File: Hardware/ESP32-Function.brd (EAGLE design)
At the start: 65 x 38.1 mm, 42 parts, among them J1 MICROMOD_STANDARD, Q2 MBT3904DW1T1, U1 EEPROM, U2 ESP-WROOM-3232D-NARROW, U3 3.3V, U4 CP210X

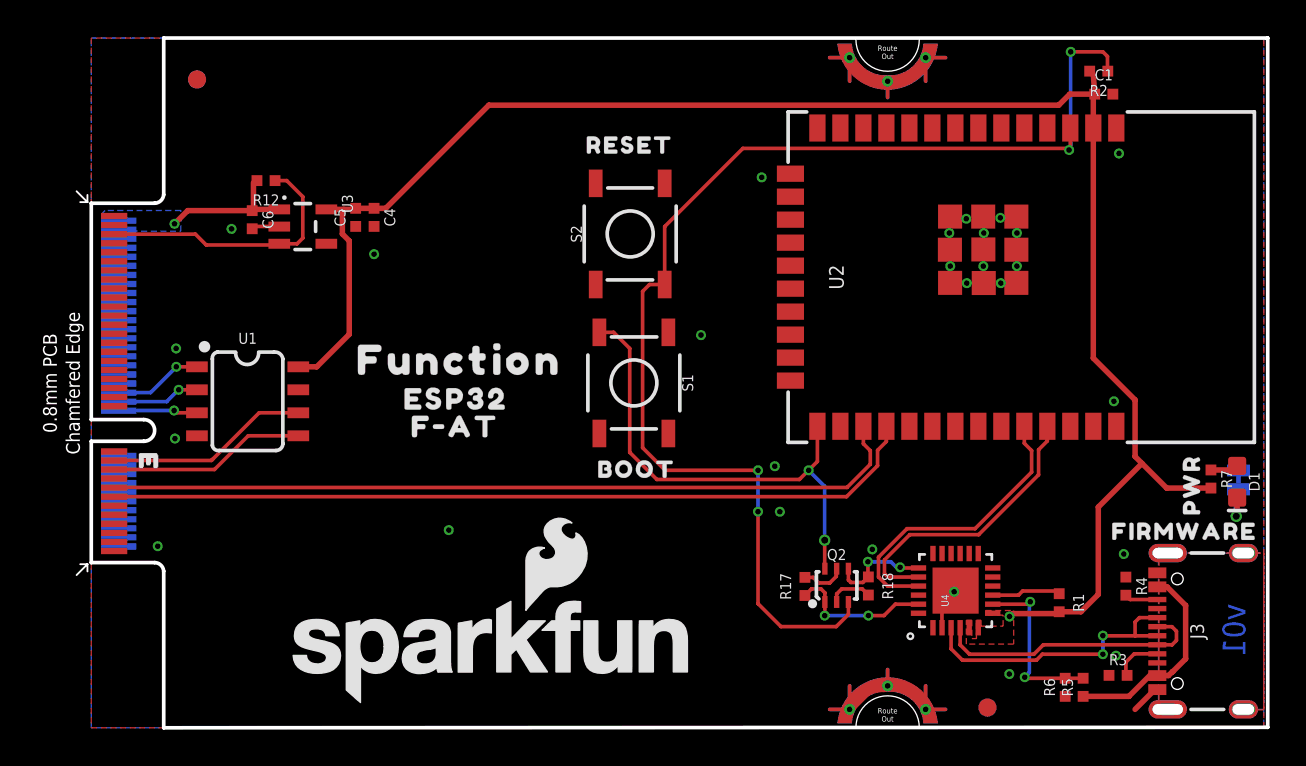
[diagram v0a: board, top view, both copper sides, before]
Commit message: Moves to 0603 components where able, adds silk, fixes traces affected by move to 0603
* removes wire stubs
* Fixes random air wires
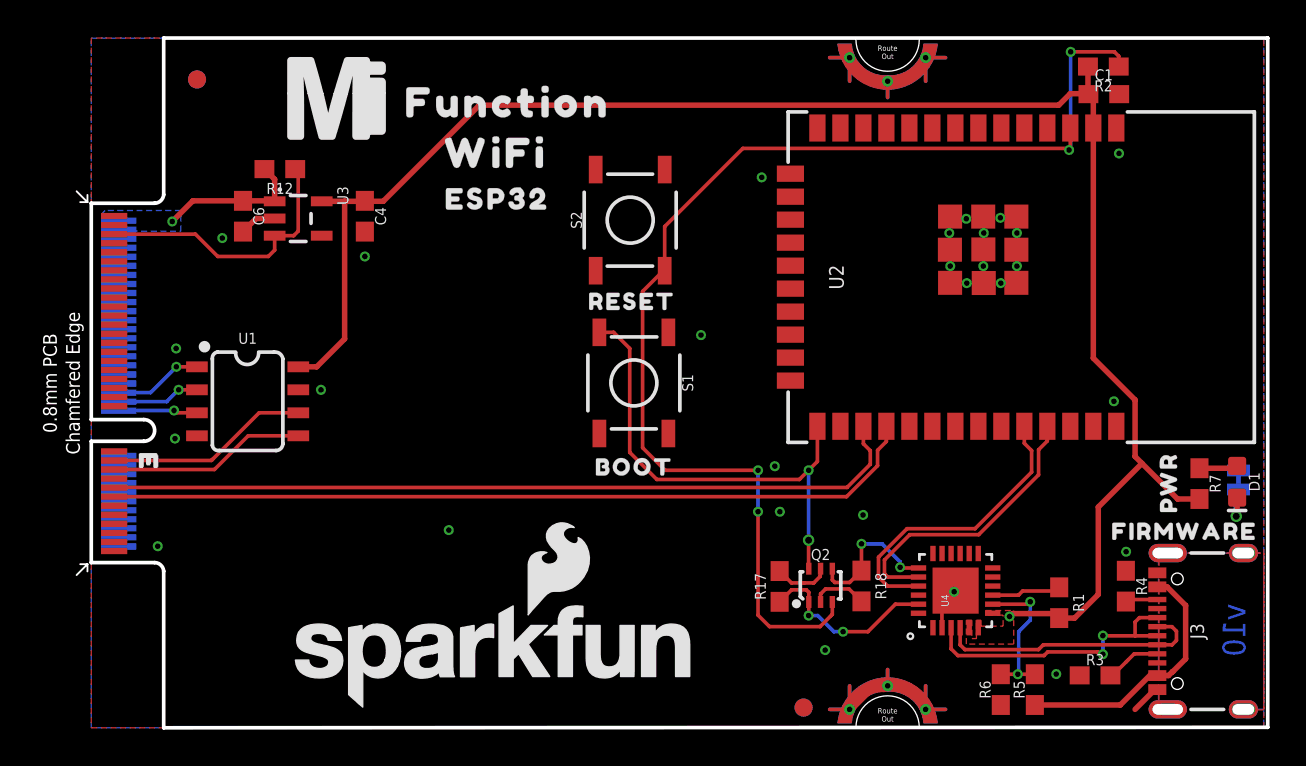
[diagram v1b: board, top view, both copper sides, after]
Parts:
- removed C5: 0.1uF, SparkFun-Capacitors:0402-TIGHT
- removed U$3: (no value), top:F#AT3213
- added U$10: (no value), top:WIFI525
- added U$6: (no value), SparkFun-MicroMod:MICROMOD_MI_LOGO_1
- C1, C6: device SparkFun-Capacitors:0402-TIGHT -> SparkFun-Capacitors:0603
- C4: value 0.1uF -> 1.0uF; device SparkFun-Capacitors:0402-TIGHT -> SparkFun-Capacitors:0603
- D1: device SparkFun-MicroMod-Function:LED-0603 -> SparkFun-LED:LED-0603
- R1, R12, R17, R18, R2, R3, R4, R5, R6, R7: device SparkFun-Resistors:0402-TIGHT -> SparkFun-Resistors:0603
- moved U$2 14.5 mm to (23.0, 34.5)
- moved U$4 11.3 mm to (22.4, 29.2)
- moved FD2 10.2 mm to (39.3, 1.12)
- moved FD4 10.2 mm to (39.3, 1.12)
- moved U$5 8.64 mm to (29.9, 23.5)
- moved R6 3.56 mm to (50.2, 2.11)
- moved R5 2.67 mm to (52.1, 2.11)
- moved R17 1.40 mm to (38.0, 7.81)
- moved U$9 1.28 mm to (59.5, 13.5)
- moved R3 1.27 mm to (55.4, 2.90)
- moved R12 0.99 mm to (10.4, 30.9)
- moved Q2 0.89 mm to (40.3, 7.87)
- moved TP2 0.89 mm to (39.6, 10.4)
- moved S2 0.76 mm to (29.8, 28.0)
- moved R7 0.68 mm to (61.2, 13.5)
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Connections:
- net 3.3V: no longer C5.2
- net GND: no longer C5.1
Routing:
- net N$3: track 11.5 -> 14.4 mm
- net DTR: track 8.05 -> 10.3 mm
- net RTS: track 5.69 -> 7.92 mm
- net N$4: track 9.67 -> 8.29 mm
- net N$12: track 2.45 -> 3.10 mm
- net N$10: track 2.44 -> 3.10 mm
- net CHIP_PU: track 67.8 -> 67.2 mm
- net N$7: track 1.54 -> 2.14 mm
- net GND: track 9.59 -> 10.1 mm, vias 27 -> 28
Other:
- board text added: "v10"
- board text removed: "v01"

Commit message: Adds I2C pullups and jumper to remove them, rearranges silk
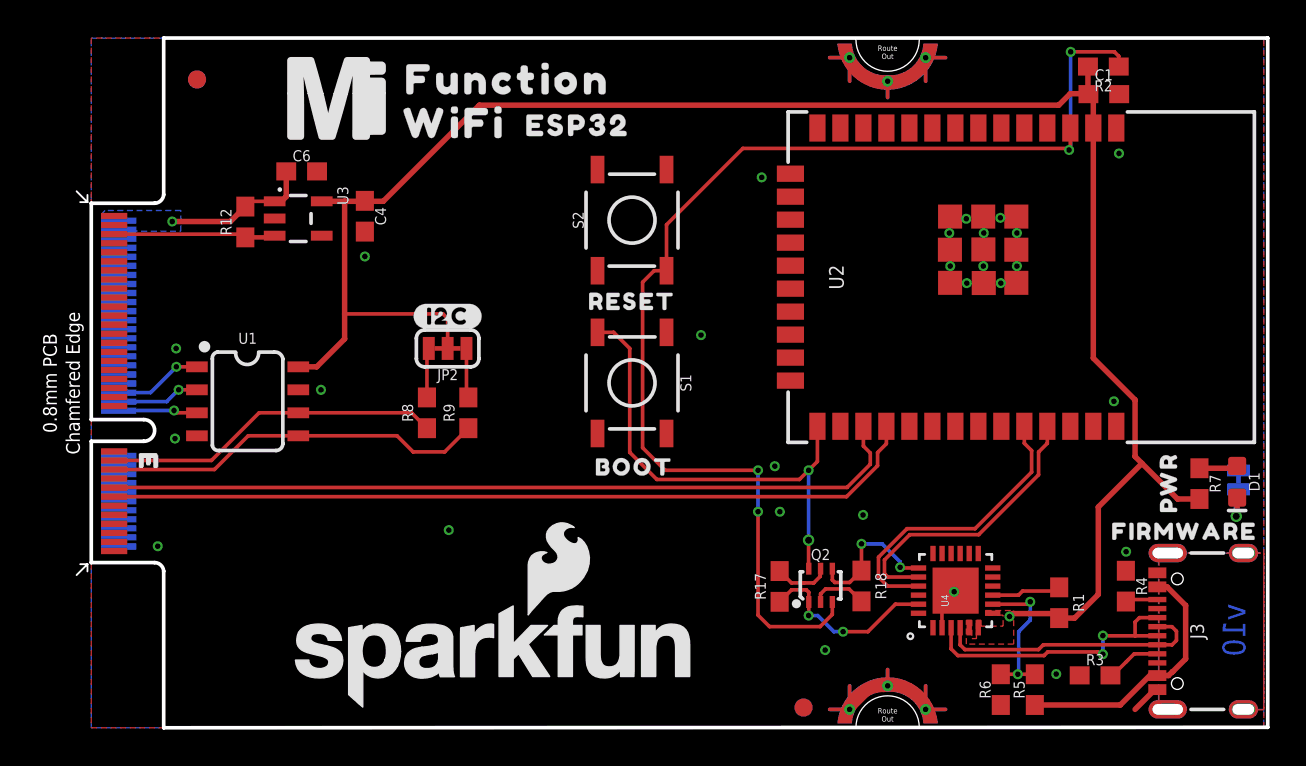
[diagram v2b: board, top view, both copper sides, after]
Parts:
- added JP2: JUMPER-SMT_3_2-NC_TRACE_SILK, SparkFun-Jumpers:SMT-JUMPER_3_2-NC_TRACE_SILK
- added R8, R9: 4.7k, SparkFun-Resistors:0603
- added U$3: (no value), top:#I2C#1321540313558
- moved U$4 6.02 mm to (26.9, 33.3)
- moved C6 4.08 mm to (11.6, 30.7), turned to 0 degrees
- moved R12 3.49 mm to (8.51, 27.9), turned to 90 degrees
- moved U$10 2.82 mm to (20.1, 33.4)
- moved U$2 1.27 mm to (23.0, 35.8)
- moved S1 0.10 mm to (29.9, 19.1)
- moved S2 0.10 mm to (29.9, 28.0)
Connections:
- new net N$13: JP2.1, R9.2
- new net N$14: JP2.3, R8.2
- net 3.3V: now also JP2.2
- net I2C_SCL: now also R8.1
- net I2C_SDA: now also R9.1
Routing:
- net I2C_SDA: track 10.9 -> 21.2 mm
- net I2C_SCL: track 11.3 -> 18.7 mm
- net 3.3V: track 96.6 -> 104.0 mm
- net EN: track 15.3 -> 9.36 mm
- net N$14: track 0.00 -> 2.75 mm
- net N$13: track 0.00 -> 2.75 mm
- net GND: track 10.1 -> 8.04 mm, vias 28 -> 27
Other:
- board text added: "Units in Inches"

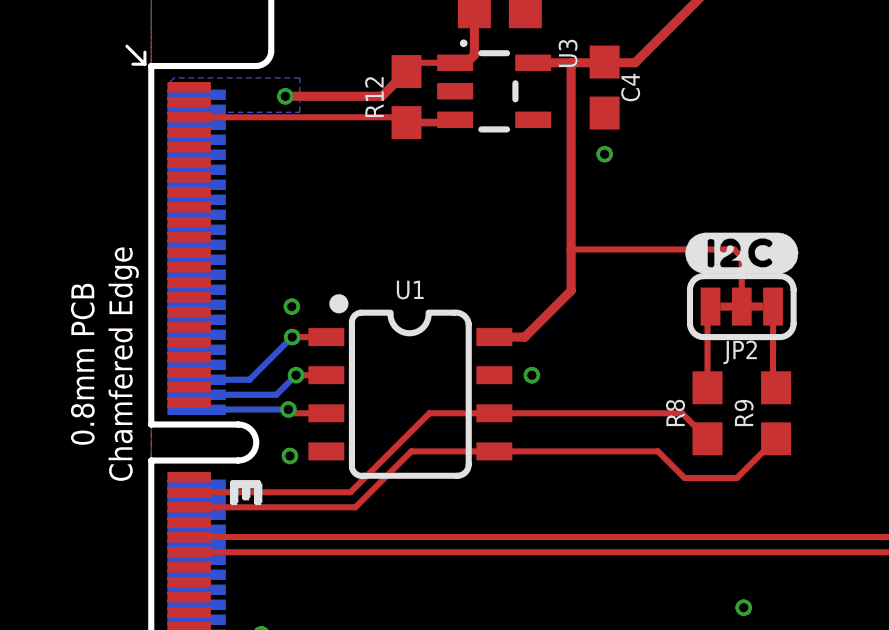
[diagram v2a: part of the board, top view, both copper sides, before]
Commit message: Adds pullup resistor and jumper to write protect net, brings write protect trace to card's edge
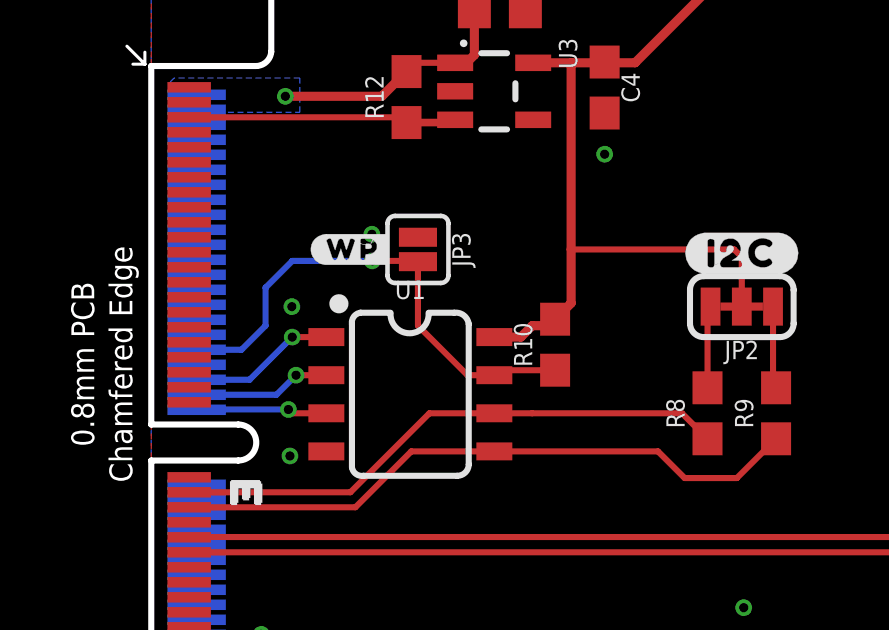
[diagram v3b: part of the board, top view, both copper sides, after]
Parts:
- added JP3: JUMPER-SMT_2_NO_SILK, SparkFun-Jumpers:SMT-JUMPER_2_NO_SILK
- added R10: 10k, SparkFun-Resistors:0603
- added U$11: (no value), top:#WP#403132222525
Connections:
- new net WP: J1.40, JP3.2, R10.1, U1.7
- net 3.3V: now also R10.2
- net GND: now also JP3.1; no longer U1.7
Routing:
- net WP: track 0.00 -> 16.8 mm, vias 0 -> 1
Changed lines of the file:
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@@
 </element>
 <element name="U$3" library="top" package="#I2C#1321540313558" value="" x="19.685" y="22.733" smashed="yes"/>
+<element name="R10" library="SparkFun-Resistors" package="0603" value="10k" x="13.462" y="19.685" smashed="yes" rot="R90">
+<attribute name="NAME" x="12.7" y="19.685" size="0.6096" layer="25" font="vector" ratio="20" rot="R90" align="bottom-center"/>
+<attribute name="PROD_ID" value="RES-00824" x="13.462" y="19.685" size="1.778" layer="27" font="vector" ratio="15" rot="R90" display="off"/>
+<attribute name="VALUE" x="14.224" y="19.685" size="0.6096" layer="27" font="vector" ratio="20" rot="R90" align="top-center"/>
+</element>
+<element name="JP3" library="SparkFun-Jumpers" package="SMT-JUMPER_2_NO_SILK" package3d_urn="urn:adsk.eagle:package:39279/1" value="JUMPER-SMT_2_NO_SILK" x="8.89" y="22.86" smashed="yes" rot="R270">
+<attribute name="NAME" x="10.033" y="22.86" size="0.6096" layer="25" font="vector" ratio="20" rot="R270" align="bottom-center"/>
+<attribute name="VALUE" x="7.747" y="22.86" size="0.6096" layer="27" font="vector" ratio="20" rot="R270" align="top-center"/>
+</element>
+<element name="U$11" library="top" package="#WP#403132222525" value="" x="6.731" y="22.86" smashed="yes"/>
 </elements>
 <signals>
@@
 <contactref element="R7" pad="2"/>
 <contactref element="U1" pad="8"/>
-<wire x1="13.9954" y1="21.4824" x2="12.452" y2="19.939" width="0.3048" layer="1"/>
-<wire x1="11.436" y1="19.939" x2="12.452" y2="19.939" width="0.3048" layer="1"/>
 <contactref element="U2" pad="2"/>
 <polygon width="0.127" layer="1" thermals="no">
@@
 <vertex x="48.3362" y="4.6228"/>
 </polygon>
-<wire x1="13.9954" y1="21.4824" x2="13.9954" y2="22.86" width="0.3048" layer="1"/>
 <wire x1="13.9954" y1="22.86" x2="13.9954" y2="29.082" width="0.3048" layer="1"/>
 <wire x1="50.7238" y1="6.1468" x2="50.8842" y2="6.3072" width="0.3048" layer="1"/>
@@
 <wire x1="19.685" y1="22.606" x2="19.685" y2="20.955" width="0.2032" layer="1"/>
 <wire x1="19.431" y1="22.86" x2="19.685" y2="22.606" width="0.2032" layer="1"/>
+<contactref element="R10" pad="2"/>
+<wire x1="13.9954" y1="21.0684" x2="13.462" y2="20.535" width="0.3048" layer="1"/>
+<wire x1="13.9954" y1="22.86" x2="13.9954" y2="21.0684" width="0.3048" layer="1"/>
+<wire x1="13.462" y1="20.535" x2="13.247" y2="20.32" width="0.3048" layer="1"/>
+<wire x1="12.7" y1="20.32" x2="13.247" y2="20.32" width="0.3048" layer="1"/>
+<wire x1="11.436" y1="19.939" x2="12.319" y2="19.939" width="0.3048" layer="1"/>
+<wire x1="12.319" y1="19.939" x2="12.7" y2="20.32" width="0.3048" layer="1"/>
 </signal>
 <signal name="GND">
@@
 <contactref element="J1" pad="39"/>
 <contactref element="J1" pad="33"/>
-<contactref element="U1" pad="7"/>
 <contactref element="U1" pad="4"/>
 <via x="4.6228" y="15.9766" extent="1-16" drill="0.3048"/>
@@
 <wire x1="43.102478125" y1="2.119415625" x2="41.9990625" y2="1.016" width="0.3048" layer="1"/>
 <via x="40.5384" y="4.2926" extent="1-16" drill="0.3048"/>
-<via x="12.687775" y="18.667621875" extent="1-16" drill="0.3048"/>
+<via x="7.353775" y="23.366621875" extent="1-16" drill="0.3048"/>
+<contactref element="JP3" pad="1"/>
 </signal>
 <signal name="EN">
@@
 <wire x1="1.2632" y1="14.766" x2="6.638" y2="14.766" width="0.2032" layer="1"/>
 <contactref element="R8" pad="1"/>
-<wire x1="11.436" y1="17.399" x2="17.692" y2="17.399" width="0.2032" layer="1"/>
+<wire x1="11.436" y1="17.399" x2="12.7" y2="17.399" width="0.2032" layer="1"/>
+<wire x1="12.7" y1="17.399" x2="17.692" y2="17.399" width="0.2032" layer="1"/>
 <wire x1="17.692" y1="17.399" x2="18.542" y2="16.549" width="0.2032" layer="1"/>
 </signal>
@@
 <wire x1="18.542" y1="20.8534" x2="18.6436" y2="20.955" width="0.2032" layer="1"/>
 </signal>
+<signal name="WP">
+<contactref element="J1" pad="40"/>
+<contactref element="U1" pad="7"/>
+<contactref element="R10" pad="1"/>
+<contactref element="JP3" pad="2"/>
+<wire x1="11.436" y1="18.669" x2="11.602" y2="18.835" width="0.2032" layer="1"/>
+<wire x1="11.602" y1="18.835" x2="13.462" y2="18.835" width="0.2032" layer="1"/>
+<wire x1="11.436" y1="18.669" x2="10.541" y2="18.669" width="0.2032" layer="1"/>
+<wire x1="8.89" y1="20.32" x2="8.89" y2="22.4536" width="0.2032" layer="1"/>
+<wire x1="10.541" y1="18.669" x2="8.89" y2="20.32" width="0.2032" layer="1"/>
+<wire x1="1.5132" y1="19.516" x2="3.006" y2="19.516" width="0.2032" layer="16"/>
+<wire x1="3.006" y1="19.516" x2="3.81" y2="20.32" width="0.2032" layer="16"/>
+<wire x1="3.81" y1="20.32" x2="3.81" y2="21.59" width="0.2032" layer="16"/>
+<wire x1="3.81" y1="21.59" x2="4.699" y2="22.479" width="0.2032" layer="16"/>
+<wire x1="4.699" y1="22.479" x2="7.366" y2="22.479" width="0.2032" layer="16"/>
+<via x="7.366" y="22.479" extent="1-16" drill="0.3048"/>
+<wire x1="7.366" y1="22.479" x2="8.8646" y2="22.479" width="0.2032" layer="1"/>
+<wire x1="8.8646" y1="22.479" x2="8.89" y2="22.4536" width="0.2032" layer="1"/>
+</signal>
 </signals>
